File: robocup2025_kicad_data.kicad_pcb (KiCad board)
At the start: 4 copper layers, 73.7 x 78.7 mm, 11 parts, among them U1 RASPBERRY_PI_4B_4GB, U2 ESP32-DEVKITC-32E

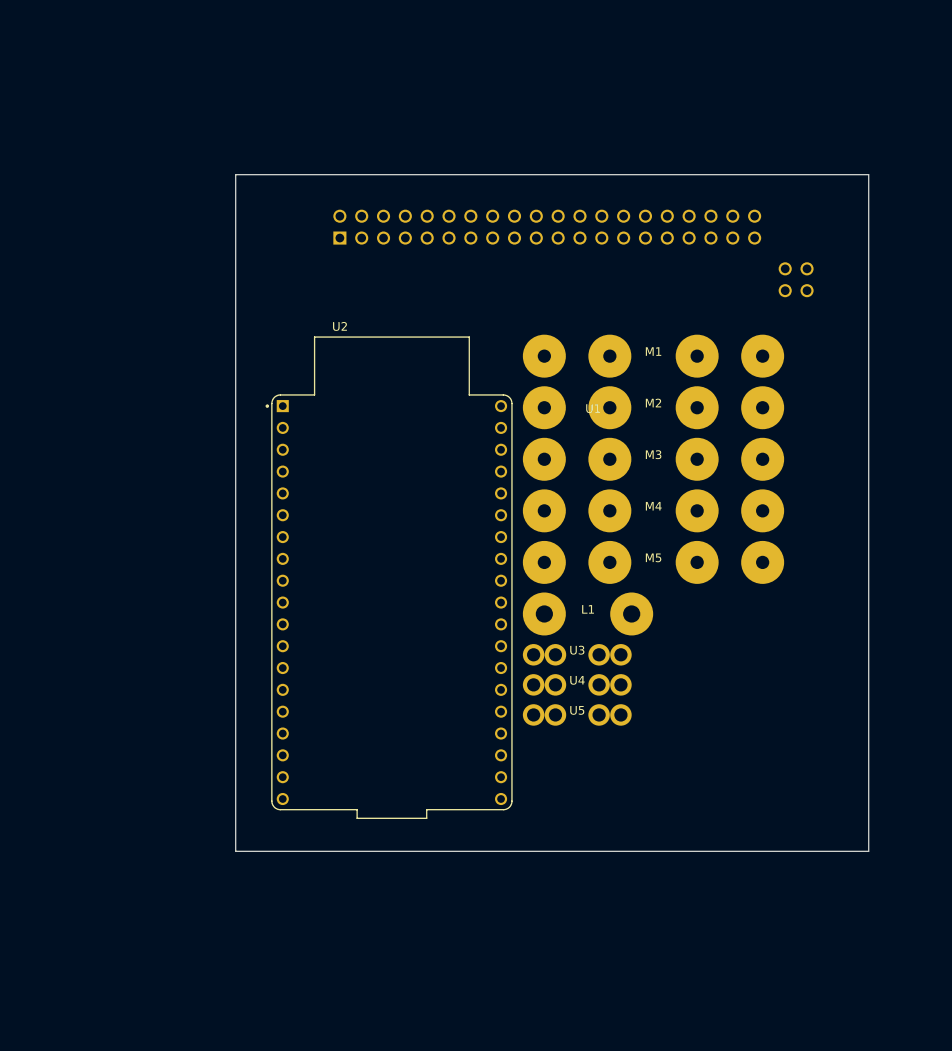
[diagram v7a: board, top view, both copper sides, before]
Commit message: make pcb and wiring. with unconnected
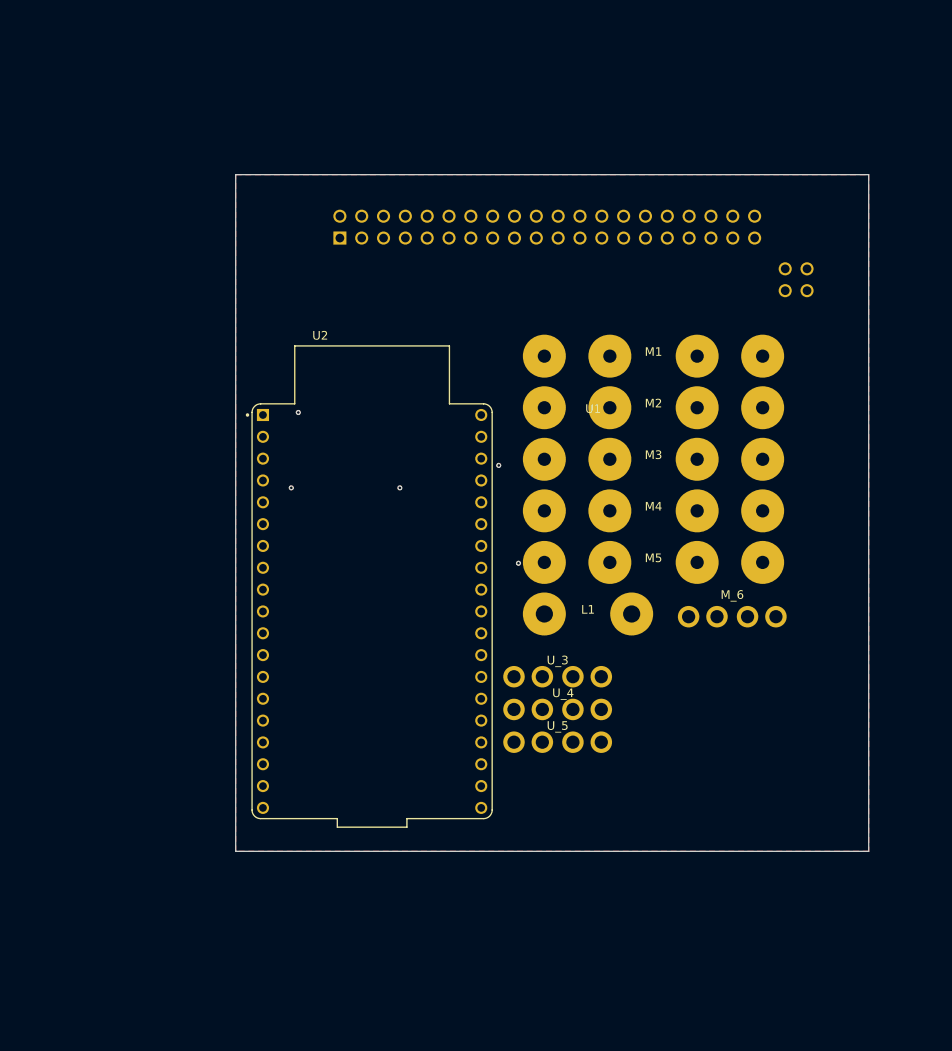
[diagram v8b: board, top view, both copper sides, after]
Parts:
- removed U3, U4, U5: ~, robo:ultrasonic
- added M_6: ~, robo:tmp, F.Cu at (164.5, 107.3)
- added U_3: ~, robo:tmp, F.Cu at (144.1, 114.3)
- added U_4: ~, robo:tmp, F.Cu at (144.1, 118.1)
- added U_5: ~, robo:tmp, F.Cu at (144.1, 121.9)
- moved U2 2.53 mm to (122.6, 106.7)
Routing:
- net rasp_5V: track 0.00 -> 115.1 mm
- net tyre_pulse_1: track 0.00 -> 95.1 mm, vias 0 -> 1
- net tyre_pulse_2: track 0.00 -> 73.6 mm, vias 0 -> 1
- net LiPo+: track 0.00 -> 51.0 mm
- net SDA: track 0.00 -> 47.1 mm, vias 0 -> 1
- net ultrasonic_echo3: track 0.00 -> 43.4 mm
- net arm_feedback: track 0.00 -> 43.3 mm
- net tyre_pulse_3: track 0.00 -> 40.3 mm, vias 0 -> 1
- net ultrasonic_echo2: track 0.00 -> 39.1 mm
- net SCL: track 0.00 -> 30.4 mm
- net ultrasonic_trig3: track 0.00 -> 24.8 mm
- net ultrasonic_echo1: track 0.00 -> 20.5 mm, vias 0 -> 1
- net tyre_pulse_4: track 0.00 -> 19.8 mm
- net ultrasonic_trig2: track 0.00 -> 16.8 mm
- net arm_pulse: track 0.00 -> 14.0 mm
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- added copper zone on F.Cu, net GND
